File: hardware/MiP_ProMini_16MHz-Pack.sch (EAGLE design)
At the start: 47 parts, among them Q1 8MHz, U1 ATMEGA328, U2 MIC5205, U3 TS3USB221A

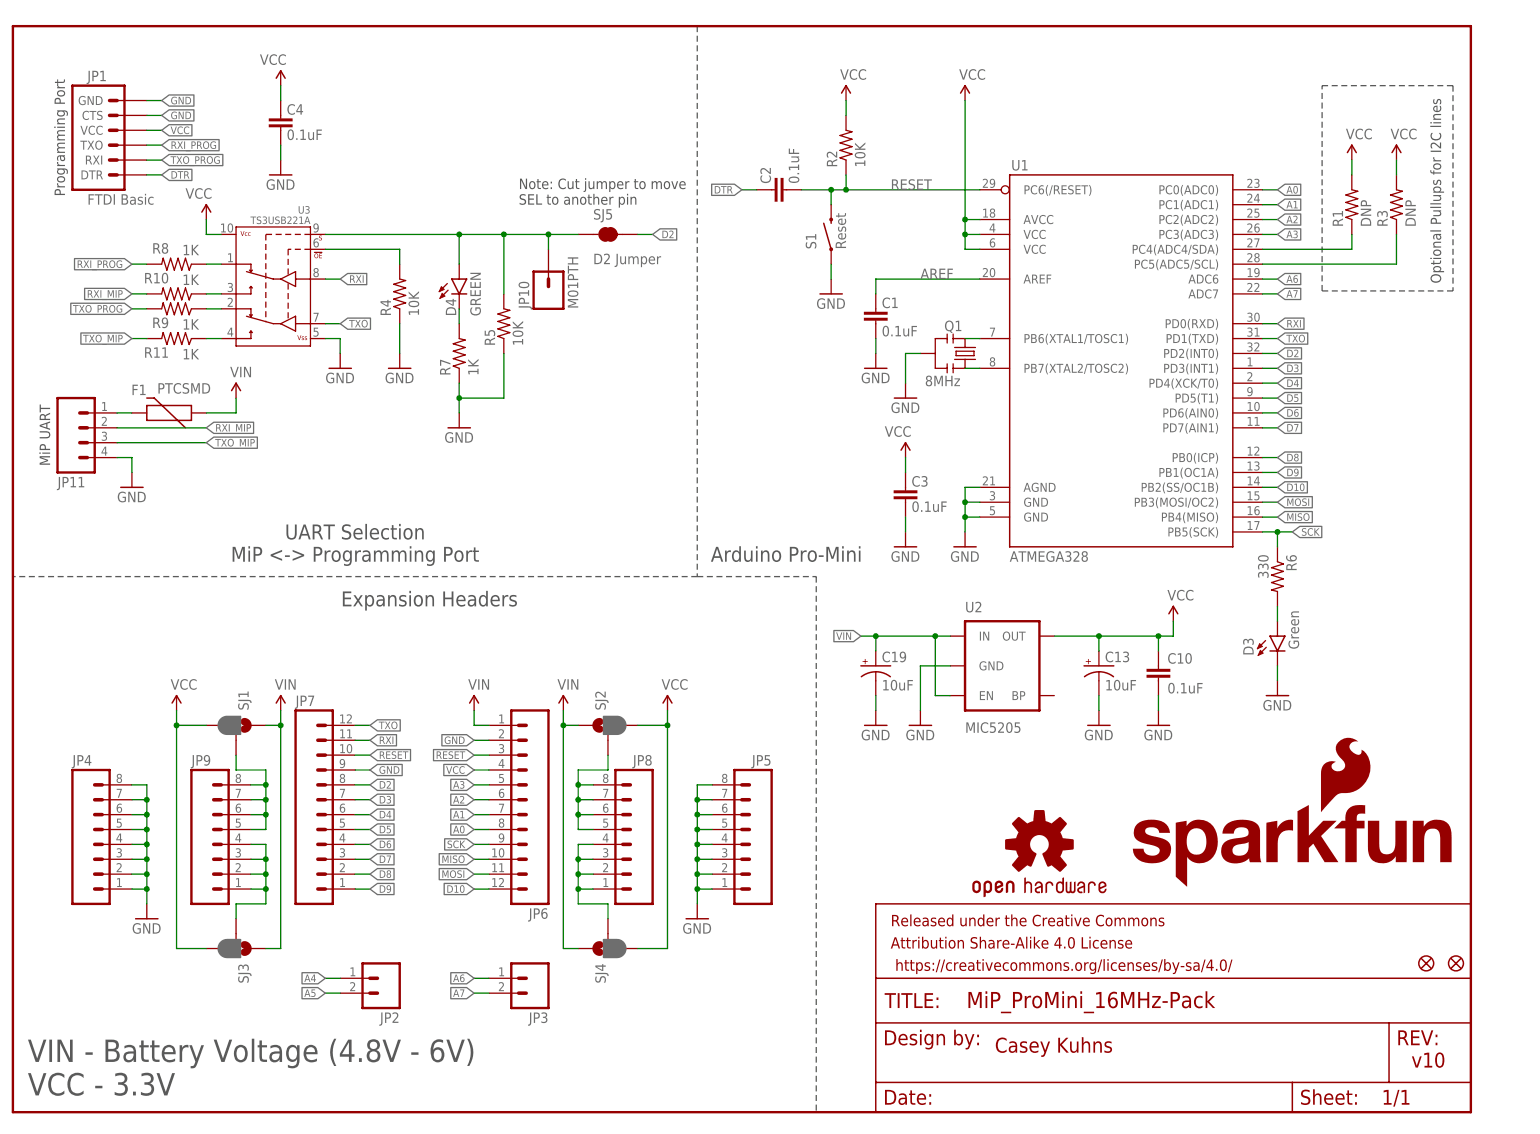
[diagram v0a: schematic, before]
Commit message: Update schematic to 16MHz / 5V
The ATMEGA328 can't reliably receive data from the MiP at 115200 bps
when running at 8MHz. This commit bumps the clock rate up to 16MHz and
bumps the voltage up to 5V so that the AVR can reliably run at this
higher rate.

Other changes to the schematic include:
* By default the VCC pin of the FTDI header is no longer connected to
  anything. This was done so that the user doesn't risk powering the
  board from both the MiP batteries and the FTDI adapter at the same
  time. It also means that the user doesn't need to worry about whether
  their FTDI adapter is configured to place 5V or 3.3V on this pin. If
  the user wants to power the board from a 5V FTDI cable when MiP
  battery power is disconnected then they can short the two pins of J1.
* The TS3USB221A switch is still powered at 3.3V. I added 1k ohm
  current limiting resistors to its inputs and also added a schottky
  diode for level conversion on the TXO pin.
* Added an AVR ISP header to make it easier to get the Arduino
  bootloader initially loaded into the ATMEGA328. The user would
  want to do this bootloader programming before C2 is installed on the
  RESET line since it will cause the programming to fail otherwise.
* I cascaded the 3.3V regulator off of the 5V supply so that the board
  will work if powered from the FTDI cable.
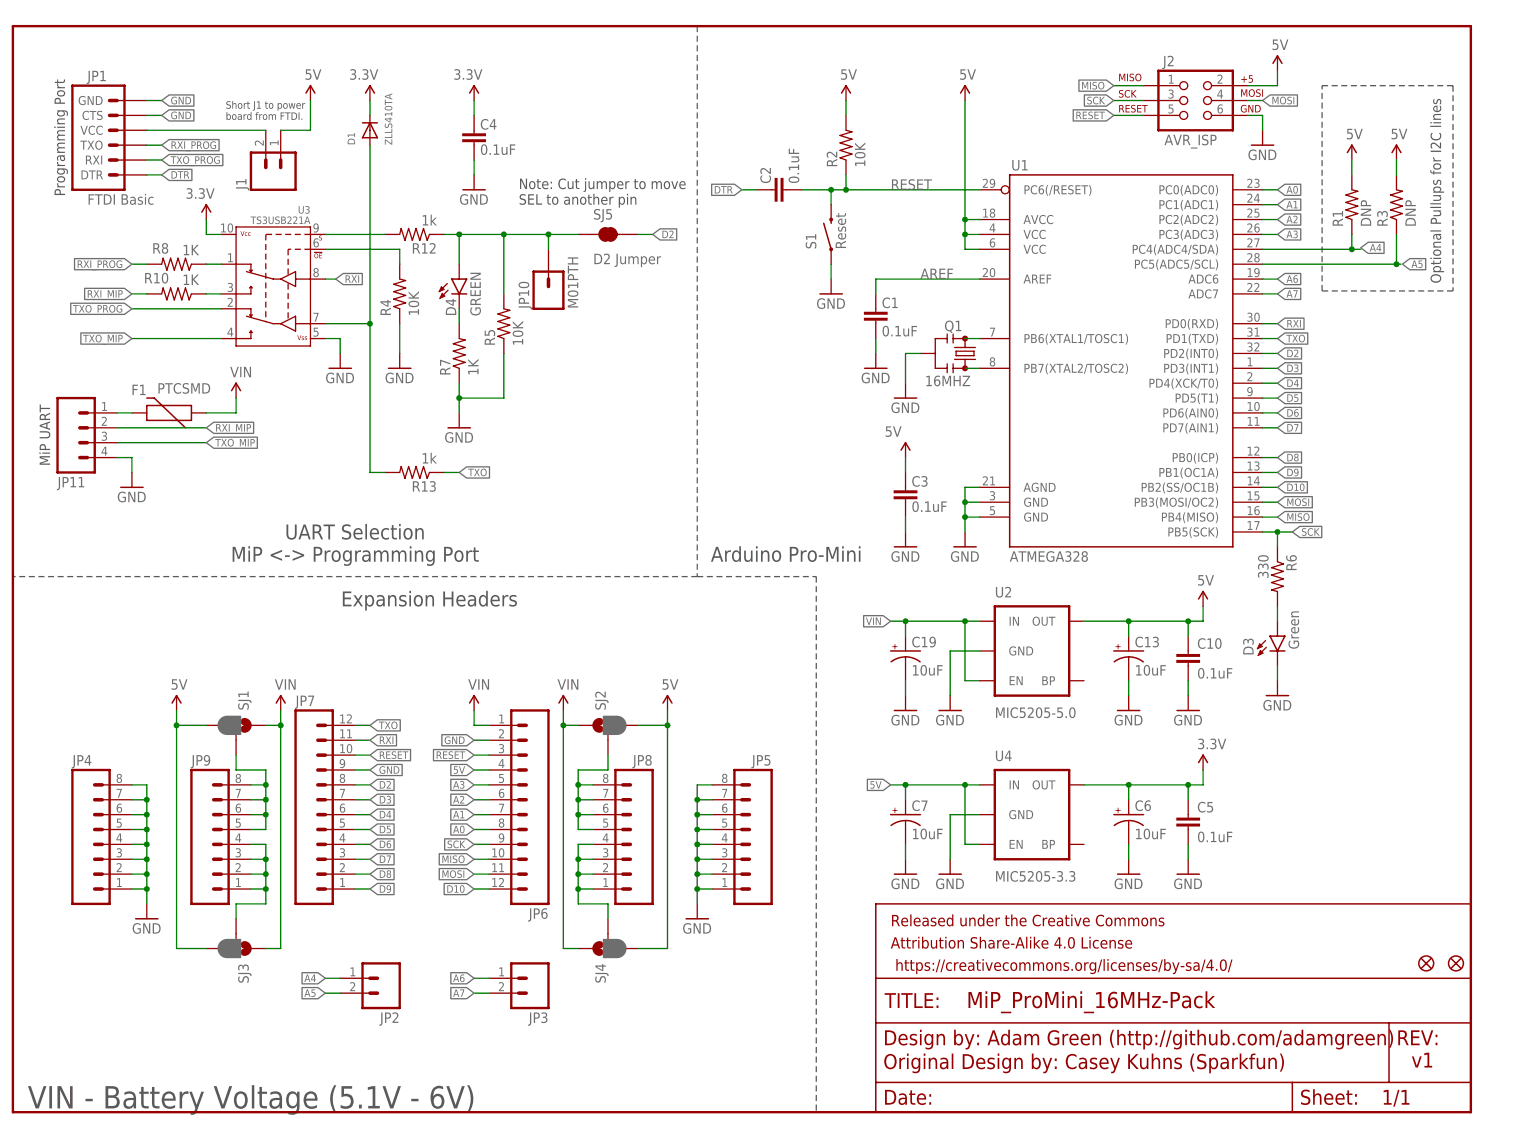
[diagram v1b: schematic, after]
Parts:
- removed LOGO1: SFE_LOGO_NAME_FLAME.1_INCH, SparkFun-Aesthetics:SFE_LOGO_NAME_FLAME.1_INCH
- removed LOGO2: OSHW-LOGOS, SparkFun-Aesthetics:OSHW-LOGOS
- removed R11, R9: 1K, SparkFun-Resistors:1KOHM1/10W1%(0603)
- added C5: 0.1uF, SparkFun-Capacitors:0.1UF-25V(+80/-20%)(0603)
- added C6, C7: 10uF, SparkFun:CAP_POL1206
- added D1: ZLLS410TA, adafruit:DIODESOD-323F
- added J1: (no value), SparkFun-Connectors:M02PTH
- added J2: AVR_ISP, SparkFun-Connectors:AVR_SPI_PRG_6PTH
- added R12, R13: 1k, SparkFun-Resistors:10KOHM1/10W1%(0603)0603
- added U4: MIC5205-3.3, SparkFun-PowerIC:MIC52053.3V
- Q1: value 8MHz -> 16MHZ; device SparkFun-FreqCtrl:RESONATOR8MHZ -> SparkFun-FreqCtrl:RESONATOR16MHZ
- U2: value MIC5205 -> MIC5205-5.0
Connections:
- removed net N$10: R11.1, U3.2D-
- removed net N$13: R9.1, U3.1D-
- removed net VCC: C10.1, C13.+, C3.2, C4.2, JP1.VCC, JP6.4, R1.2, R2.2, R3.2, SJ1.3, SJ2.3, SJ3.3, SJ4.3, U1.AVCC, U1.VCC@1, U1.VCC@2, U2.OUT, U3.VCC
- new net 3.3V: C4.2, C5.1, C6.+, D1.C, U3.VCC, U4.OUT
- new net 5V: C10.1, C13.+, C3.2, C7.+, J1.1, J2.2, JP6.4, R1.2, R2.2, R3.2, SJ1.3, SJ2.3, SJ3.3, SJ4.3, U1.AVCC, U1.VCC@1, U1.VCC@2, U2.OUT, U4.EN, U4.IN
- new net N$15: J1.2, JP1.VCC
- new net N$16: R12.2, U3.S
- new net N$18: D1.A, R13.2, U3.D-
- net GND: now also C5.2, C6.-, C7.-, J2.6, U4.GND
- net MISO: now also J2.1
- net MOSI: now also J2.4
- net RESET: now also J2.5
- net SCK: now also J2.3
- net SELECT: now also R12.1; no longer U3.S
- net TXO: now also R13.1; no longer U3.D-
- net TXO_MIP: now also U3.2D-; no longer R11.2
- net TXO_PROG: now also U3.1D-; no longer R9.2
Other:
- note added: "Adam Green (http://github.com/adamgreen)"
- note added: "Original Design by: Casey Kuhns (Sparkfun)"
- note added: "Short J1 to power board from FTDI."
- note added: "VIN - Battery Voltage (5.1V - 6V)"
- note added: "v1"
- note removed: "Casey Kuhns"
- note removed: "VIN - Battery Voltage (4.8V - 6V) VCC - 3.3V"
- note removed: "v10"
- moved on the sheet: C10, C13, C19, C4, U2

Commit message: Add 3.3V to headers for v2
Revision 2 of the schematic now allows the lower portion of the
vertical power buses to be selected between 3.3V and 6V while the upper
portion can be selected between 5V and 6V. Previously only the
regulated 5V and unregulated 6V were available for prototyping but it
makes sense to expose the regulated 3.3V as well incase the user wants
to use 3.3V peripherals.
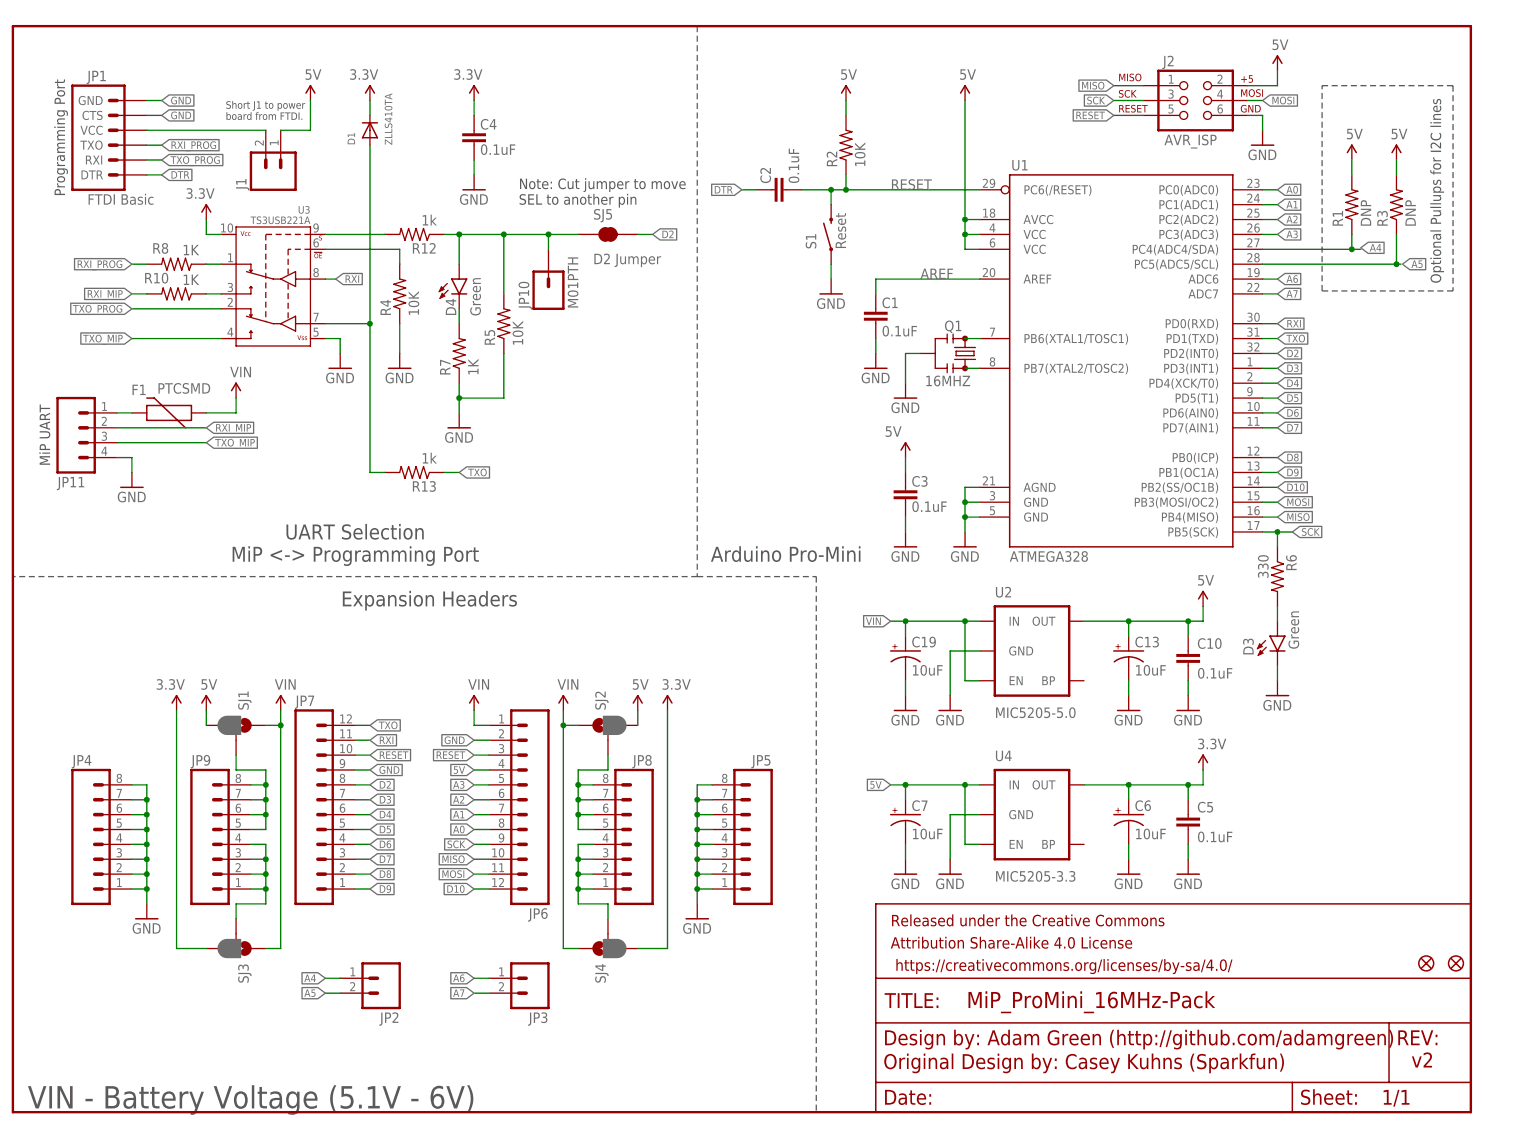
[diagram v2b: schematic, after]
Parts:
- D4: value GREEN -> Green
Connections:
- net 3.3V: now also SJ3.3, SJ4.3
- net 5V: no longer SJ3.3, SJ4.3
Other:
- note added: "v2"
- note removed: "v1"
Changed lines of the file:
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@@
 <part name="GND9" library="SparkFun-Aesthetics" deviceset="GND" device=""/>
 <part name="GND10" library="SparkFun-Aesthetics" deviceset="GND" device=""/>
-<part name="D4" library="SparkFun-LED" deviceset="LED-GREEN" device="0603" value="GREEN"/>
+<part name="D4" library="SparkFun-LED" deviceset="LED-GREEN" device="0603" value="Green"/>
 <part name="R7" library="SparkFun-Resistors" deviceset="1KOHM1/10W1%(0603)" device="" value="1K"/>
 <part name="SUPPLY3" library="SparkFun-Aesthetics" deviceset="VIN" device=""/>
@@
 <part name="P+13" library="SparkFun-Aesthetics" deviceset="5V" device="" value="5V"/>
 <part name="R10" library="SparkFun-Resistors" deviceset="1KOHM1/10W1%(0603)" device="" value="1K"/>
+<part name="P+14" library="SparkFun-Aesthetics" deviceset="3.3V" device="" value="3.3V"/>
+<part name="P+16" library="SparkFun-Aesthetics" deviceset="3.3V" device="" value="3.3V"/>
 </parts>
 <sheets>
@@
 <text x="243.84" y="141.478" size="1.778" layer="97" rot="R90">Optional Pullups for I2C lines</text>
 <text x="166.37" y="11.43" size="2.54" layer="94">Adam Green (http://github.com/adamgreen)</text>
-<text x="238.76" y="7.62" size="2.54" layer="94">v1</text>
+<text x="238.76" y="7.62" size="2.54" layer="94">v2</text>
 <text x="86.36" y="154.94" size="1.778" layer="97">Note: Cut jumper to move
 SEL to another pin</text>
@@
 <instance part="SJ2" gate="G$1" x="101.6" y="66.04" rot="R90"/>
 <instance part="SJ4" gate="G$1" x="101.6" y="27.94" rot="MR270"/>
-<instance part="P+4" gate="G$1" x="27.94" y="68.58"/>
-<instance part="P+5" gate="G$1" x="111.76" y="68.58"/>
+<instance part="P+4" gate="G$1" x="33.02" y="68.58"/>
+<instance part="P+5" gate="G$1" x="106.68" y="68.58"/>
 <instance part="SUPPLY1" gate="G$1" x="93.98" y="68.58"/>
 <instance part="SUPPLY2" gate="G$1" x="45.72" y="68.58"/>
@@
 <attribute name="NAME" x="26.67" y="143.2814" size="1.778" layer="95" rot="R180"/>
 <attribute name="VALUE" x="31.75" y="143.002" size="1.778" layer="96" rot="R180"/>
+</instance>
+<instance part="P+14" gate="G$1" x="27.94" y="68.58" smashed="yes">
+<attribute name="VALUE" x="24.384" y="72.136" size="1.778" layer="96"/>
+</instance>
+<instance part="P+16" gate="G$1" x="111.76" y="68.58" smashed="yes">
+<attribute name="VALUE" x="110.744" y="72.136" size="1.778" layer="96"/>
 </instance>
 </instances>
@@
 </segment>
 <segment>
-<wire x1="33.02" y1="27.94" x2="27.94" y2="27.94" width="0.1524" layer="91"/>
-<wire x1="27.94" y1="27.94" x2="27.94" y2="66.04" width="0.1524" layer="91"/>
-<wire x1="27.94" y1="66.04" x2="33.02" y2="66.04" width="0.1524" layer="91"/>
-<pinref part="P+4" gate="G$1" pin="5V"/>
-<wire x1="27.94" y1="68.58" x2="27.94" y2="66.04" width="0.1524" layer="91"/>
-<junction x="27.94" y="66.04"/>
-<pinref part="SJ1" gate="G$1" pin="3"/>
-<pinref part="SJ3" gate="G$1" pin="3"/>
-</segment>
-<segment>
-<pinref part="SJ4" gate="G$1" pin="3"/>
-<wire x1="106.68" y1="27.94" x2="111.76" y2="27.94" width="0.1524" layer="91"/>
-<wire x1="111.76" y1="27.94" x2="111.76" y2="66.04" width="0.1524" layer="91"/>
-<pinref part="SJ2" gate="G$1" pin="3"/>
-<wire x1="111.76" y1="66.04" x2="106.68" y2="66.04" width="0.1524" layer="91"/>
-<pinref part="P+5" gate="G$1" pin="5V"/>
-<wire x1="111.76" y1="68.58" x2="111.76" y2="66.04" width="0.1524" layer="91"/>
-<junction x="111.76" y="66.04"/>
-</segment>
-<segment>
 <pinref part="P+8" gate="G$1" pin="5V"/>
 <wire x1="203.2" y1="86.36" x2="203.2" y2="83.82" width="0.1524" layer="91"/>
@@
 <wire x1="215.9" y1="175.26" x2="215.9" y2="177.8" width="0.1524" layer="91"/>
 </segment>
+<segment>
+<pinref part="P+4" gate="G$1" pin="5V"/>
+<pinref part="SJ1" gate="G$1" pin="3"/>
+<wire x1="33.02" y1="68.58" x2="33.02" y2="66.04" width="0.1524" layer="91"/>
+</segment>
+<segment>
+<pinref part="SJ2" gate="G$1" pin="3"/>
+<pinref part="P+5" gate="G$1" pin="5V"/>
+<wire x1="106.68" y1="66.04" x2="106.68" y2="68.58" width="0.1524" layer="91"/>
+</segment>
 </net>
 <net name="3.3V" class="0">
@@
 <wire x1="60.96" y1="170.18" x2="60.96" y2="172.72" width="0.1524" layer="91"/>
 </segment>
-</net>
+<segment>
+<pinref part="P+14" gate="G$1" pin="3.3V"/>
+<pinref part="SJ3" gate="G$1" pin="3"/>
+<wire x1="27.94" y1="68.58" x2="27.94" y2="27.94" width="0.1524" layer="91"/>
+<wire x1="27.94" y1="27.94" x2="33.02" y2="27.94" width="0.1524" layer="91"/>
+</segment>
+<segment>
+<pinref part="SJ4" gate="G$1" pin="3"/>
+<pinref part="P+16" gate="G$1" pin="3.3V"/>
+<wire x1="106.68" y1="27.94" x2="111.76" y2="27.94" width="0.1524" layer="91"/>
+<wire x1="111.76" y1="27.94" x2="111.76" y2="68.58" width="0.1524" layer="91"/>
+</segment>
+</net>
